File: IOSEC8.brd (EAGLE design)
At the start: 133 x 40 mm, 27 parts

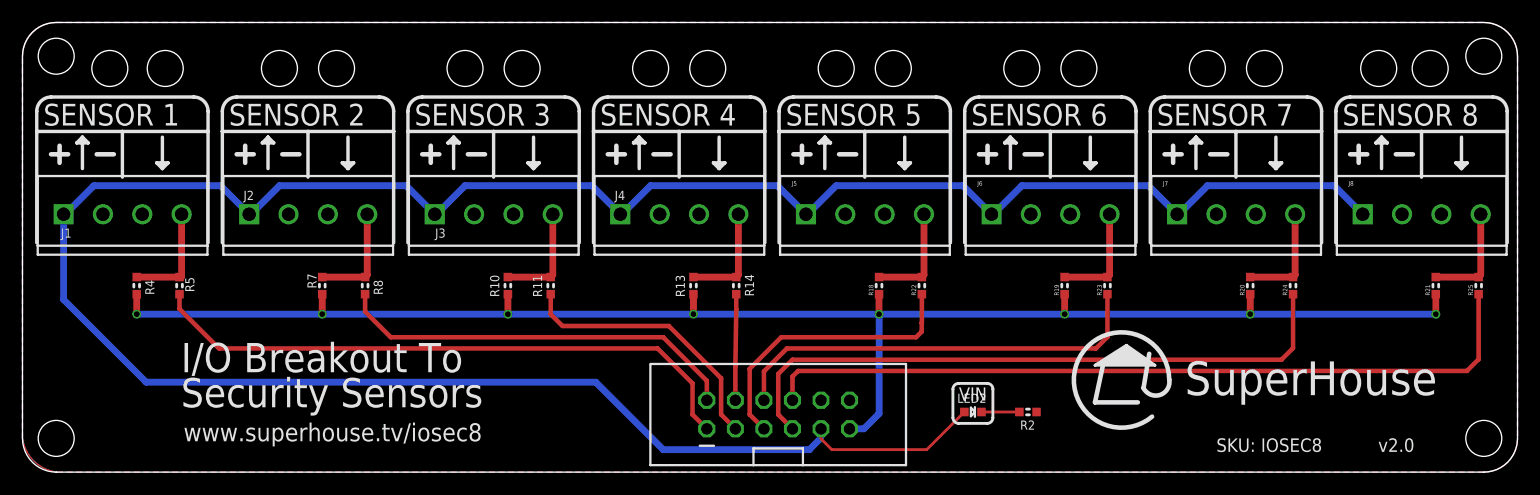
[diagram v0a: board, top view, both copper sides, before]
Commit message: Added second IO port for status LEDs. Ready for v3.0 release
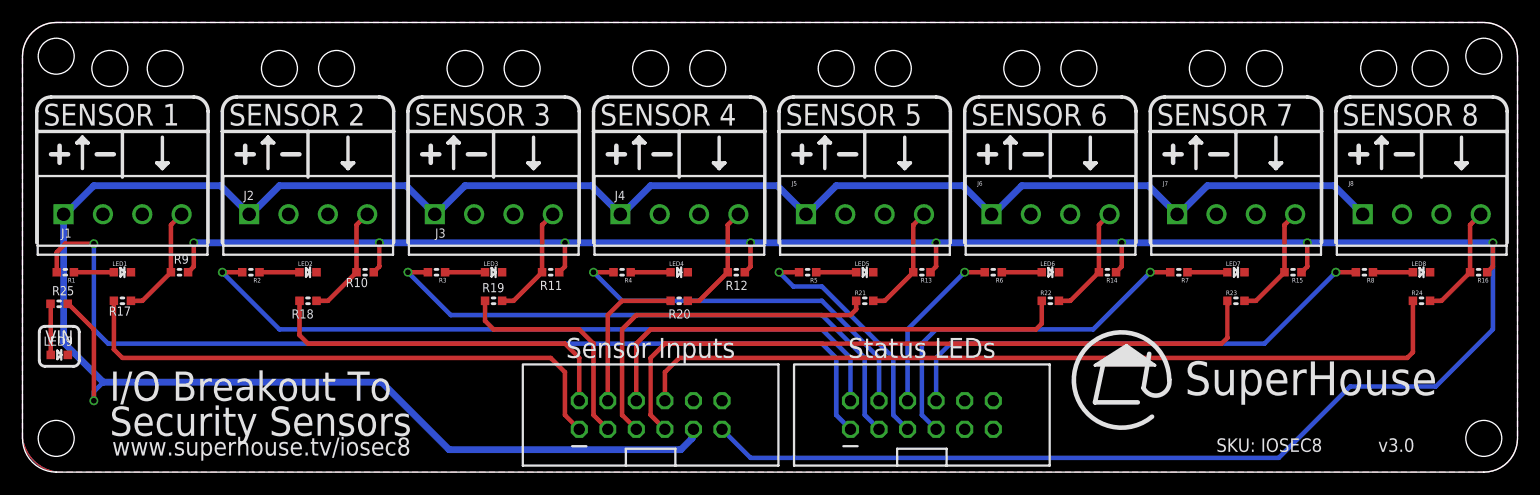
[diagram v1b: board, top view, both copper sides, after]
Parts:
- added JP2: M06X2, freetronics-jon:2X6-SHROUDED
- added LED1, LED3, LED4, LED5, LED6, LED7, LED8: RED, freetronics-jon:LED-0603
- added LED9: GREEN, freetronics-jon:LED-0603
- added R1, R17, R3, R6: 1K, freetronics-jon:0603
- added R12, R15, R16, R9: 4K7, freetronics-jon:0603
- LED2: value GREEN -> RED
- R11, R14: value 1K -> 4K7
- R18, R19, R20, R21, R4, R7: value 4K7 -> 1K
- moved R25 126.3 mm to (3.26, 15.0), turned to 0 degrees
- moved R8 88.9 mm to (119.4, 17.8), turned to 180 degrees
- moved R7 76.2 mm to (102.9, 17.8), turned to 180 degrees
- moved R2 70.2 mm to (20.3, 17.8)
- moved LED2 60.4 mm to (25.4, 17.8)
- moved R5 55.9 mm to (69.8, 17.8), turned to 180 degrees
- moved R18 50.8 mm to (25.4, 15.2), turned to 0 degrees
- moved R19 50.8 mm to (41.9, 15.2), turned to 0 degrees
- moved R20 50.8 mm to (58.4, 15.2), turned to 0 degrees
- moved R21 50.8 mm to (74.9, 15.2), turned to 0 degrees
- moved R4 43.2 mm to (53.3, 17.8), turned to 180 degrees
- moved R14 33.0 mm to (96.5, 17.8), turned to 180 degrees
- moved R13 20.4 mm to (80.0, 17.8), turned to 180 degrees
- moved R10 12.8 mm to (30.5, 17.8), turned to 180 degrees
- moved R23 11.5 mm to (108.0, 15.2), turned to 0 degrees
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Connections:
- new net L1: JP2.1, R1.2
- new net L2: JP2.2, R2.2
- new net L3: JP2.3, R3.2
- new net L4: JP2.4, R4.2
- new net L5: JP2.5, R5.2
- new net L6: JP2.6, R6.2
- new net L7: JP2.7, R7.2
- new net L8: JP2.8, R8.2
- new net N$16: LED2.A, R2.1
- new net N$17: LED3.A, R3.1
- new net N$18: LED4.A, R4.1
- new net N$19: LED5.A, R5.1
- new net N$2: LED1.A, R1.1
- new net N$20: LED6.A, R6.1
- new net N$21: LED7.A, R7.1
- new net N$22: LED8.A, R8.1
- net GND: now also JP2.10, LED1.C, LED2.C, LED3.C, LED4.C, LED5.C, LED6.C, LED7.C, LED8.C, LED9.C; no longer R2.1
- net IO1: now also R17.1; no longer R5.1
- net IO2: now also R18.1; no longer R8.1
- net IO3: now also R19.1; no longer R11.1
- net IO4: now also R20.1; no longer R14.1
- net IO5: now also R21.1; no longer R22.1
- net IO6: now also R22.1; no longer R23.1
- net IO7: now also R23.1; no longer R24.1
- net IO8: now also R24.1; no longer R25.1
- net IOREF: now also R11.1, R12.1, R14.1, R15.1, R16.1, R9.1; no longer R18.1, R19.1, R20.1, R21.1, R4.1, R7.1
- net N$1: now also LED9.A, R25.1; no longer LED2.C, R2.2
- net N$10: now also R16.2, R24.2; no longer R21.2, R25.2
- net N$249: now also R19.2; no longer R10.2
- net N$256: now also R12.2, R20.2; no longer R13.2, R14.2
- net N$262: now also R17.2, R9.2; no longer R4.2, R5.2
- net N$3: now also R10.2, R18.2; no longer R7.2, R8.2
- net N$7: now also R13.2, R21.2; no longer R18.2, R22.2
- net N$8: now also R14.2, R22.2; no longer R19.2, R23.2
- net N$9: now also R15.2, R23.2; no longer R20.2, R24.2
- net VIN: now also R25.2; no longer LED2.A
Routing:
- net L1: track 0.00 -> 87.0 mm, vias 0 -> 1
- net IOREF: track 141.8 -> 220.3 mm
- net L2: track 0.00 -> 64.6 mm, vias 0 -> 1
- net L3: track 0.00 -> 52.5 mm, vias 0 -> 1
- net L8: track 0.00 -> 44.3 mm, vias 0 -> 1
- net L4: track 0.00 -> 34.1 mm, vias 0 -> 1
- net L7: track 0.00 -> 32.9 mm, vias 0 -> 1
- net L5: track 0.00 -> 22.0 mm, vias 0 -> 1
- net L6: track 0.00 -> 15.3 mm, vias 0 -> 1
- net VIN: track 227.5 -> 214.5 mm, vias 0 -> 1
- net IO5: track 25.9 -> 31.7 mm
- net IO6: track 38.2 -> 43.9 mm
- net IO7: track 57.0 -> 62.2 mm
- net IO8: track 69.6 -> 74.4 mm
- net IO4: track 9.44 -> 13.7 mm
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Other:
- board text added: "(c) 2018 SuperHouse Automation Pty Ltd"
- board text added: "Sensor Inputs"
- board text added: "Status LEDs"
- board text added: "v3.0"
- board text removed: "(c) 2017 SuperHouse Automation Pty Ltd"
- board text removed: "v2.0"
